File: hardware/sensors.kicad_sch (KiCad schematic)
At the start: 12 parts, among them U5 MMC5983MA, U6 MS560702BA03-50, U7 ADXL375BCCZ, U8 IIM-42653

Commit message: Added digikey part numbers; usb trace width update
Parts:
- C28, C32, C33, C35: Digikey Part Number (none) -> 1276-1857-1-ND
- C29: Digikey Part Number (none) -> 311-1868-1-ND
- C30: Digikey Part Number (none) -> 490-10748-1-ND
- C31: Digikey Part Number (none) -> 478-KGM15AR51E103KTCT-ND
- C34: Digikey Part Number (none) -> 1276-2955-1-ND
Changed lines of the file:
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@@
+			)
+		)
+		(property "Digikey Part Number" "311-1868-1-ND"
+			(at 163.83 63.5 0)
+			(effects
+				(font
+					(size 1.27 1.27)
+				)
+				(hide yes)
 			)
 		)
@@
 			)
 		)
+		(property "Digikey Part Number" "1276-1857-1-ND"
+			(at 153.67 135.89 0)
+			(effects
+				(font
+					(size 1.27 1.27)
+				)
+				(hide yes)
+			)
+		)
 		(pin "1"
 		)
@@
 			)
 		)
+		(property "Digikey Part Number" "1276-2955-1-ND"
+			(at 116.84 132.08 0)
+			(effects
+				(font
+					(size 1.27 1.27)
+				)
+				(hide yes)
+			)
+		)
 		(pin "1"
 		)
@@
 			)
 		)
+		(property "Digikey Part Number" "478-KGM15AR51E103KTCT-ND"
+			(at 97.79 113.03 0)
+			(effects
+				(font
+					(size 1.27 1.27)
+				)
+				(hide yes)
+			)
+		)
 		(pin "1"
 		)
@@
 			)
 		)
+		(property "Digikey Part Number" "1276-1857-1-ND"
+			(at 45.72 60.96 0)
+			(effects
+				(font
+					(size 1.27 1.27)
+				)
+				(hide yes)
+			)
+		)
 		(pin "1"
 		)
@@
 			)
 		)
+		(property "Digikey Part Number" "1276-1857-1-ND"
+			(at 106.68 132.08 0)
+			(effects
+				(font
+					(size 1.27 1.27)
+				)
+				(hide yes)
+			)
+		)
 		(pin "1"
 		)
@@
 			)
 		)
+		(property "Digikey Part Number" "490-10748-1-ND"
+			(at 228.6 68.58 0)
+			(effects
+				(font
+					(size 1.27 1.27)
+				)
+				(hide yes)
+			)
+		)
 		(pin "1"
 		)
@@
 			)
 		)
+		(property "Digikey Part Number" "1276-1857-1-ND"
+			(at 144.78 130.81 0)
+			(effects
+				(font
+					(size 1.27 1.27)
+				)
+				(hide yes)
+			)
+		)

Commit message: Removed bad GND connection to reserved pin on ADXL375 IMU; first error found in first batch
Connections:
- net GND: no longer U7.11 (RESERVED), U7.3 (RESERVED)
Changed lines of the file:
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@@
-	)
-	(junction
-		(at 233.68 137.16)
-		(diameter 0)
-		(color 0 0 0 0)
 	)
 	(junction
@@
 		(color 0 0 0 0)
 	)
-	(junction
-		(at 233.68 139.7)
-		(diameter 0)
-		(color 0 0 0 0)
-	)
 	(wire
 		(pts
@@
 	(wire
 		(pts
-			(xy 233.68 134.62) (xy 233.68 137.16)
+			(xy 233.68 134.62) (xy 233.68 139.7)
 		)
 		(stroke
@@
 	(wire
 		(pts
-			(xy 233.68 137.16) (xy 233.68 139.7)
-		)
-		(stroke
-			(width 0)
-			(type default)
-		)
-	)
-	(wire
-		(pts
 			(xy 29.21 156.21) (xy 30.48 156.21)
 		)
@@
 	(wire
 		(pts
-			(xy 227.33 139.7) (xy 233.68 139.7)
-		)
-		(stroke
-			(width 0)
-			(type default)
-		)
-	)
-	(wire
-		(pts
 			(xy 45.72 55.88) (xy 58.42 55.88)
 		)
@@
 		)
 		(stroke
-			(width 0)
-			(type default)
-		)
-	)
-	(wire
-		(pts
-			(xy 227.33 137.16) (xy 233.68 137.16)
-		)
-		(stroke

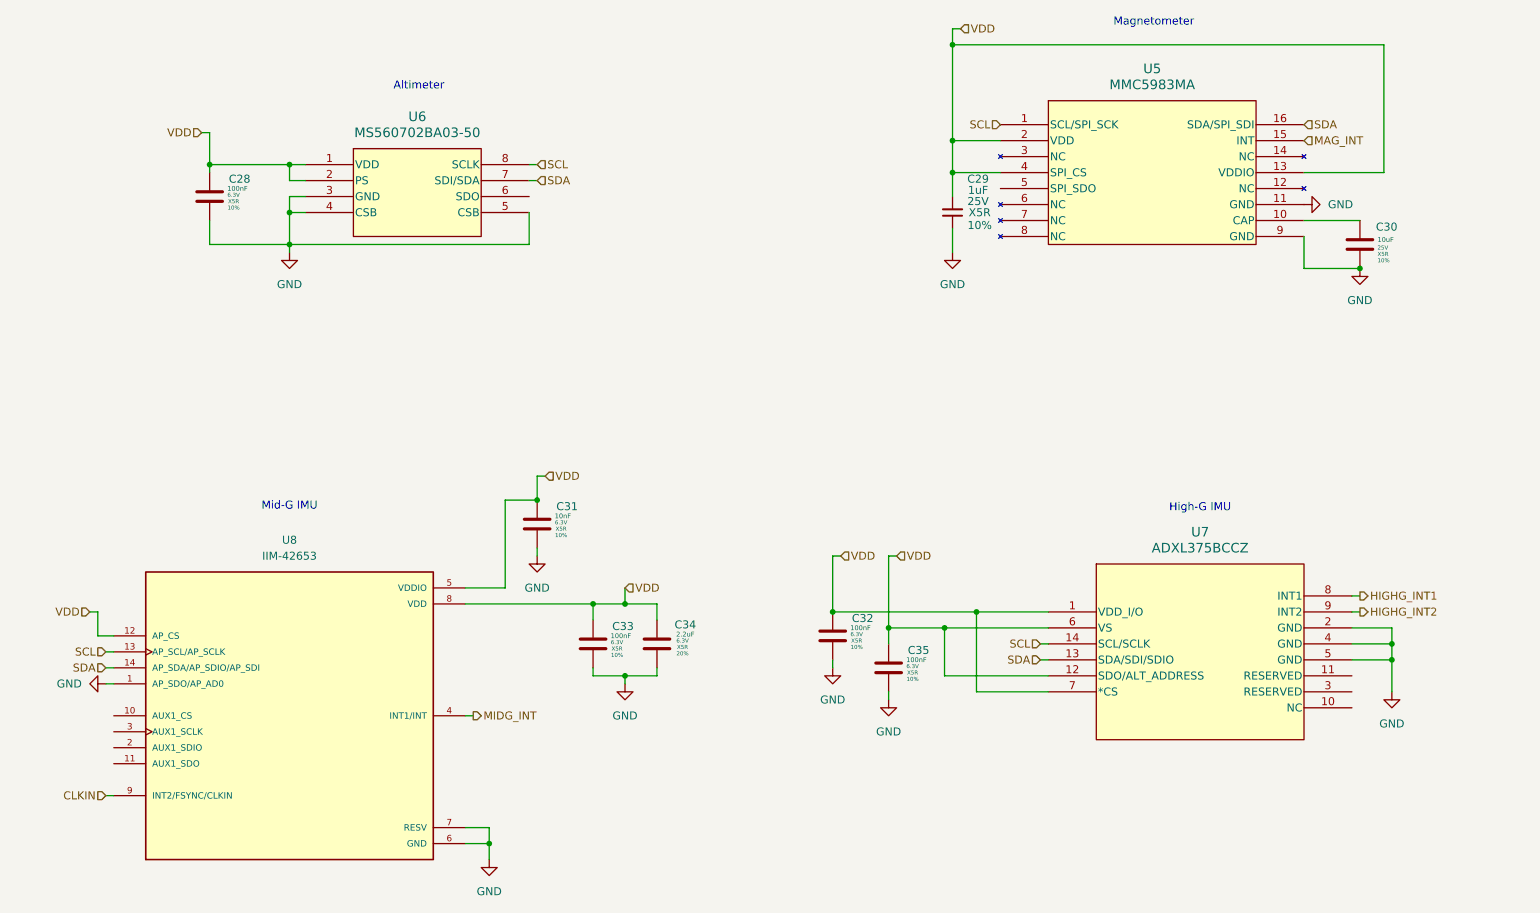
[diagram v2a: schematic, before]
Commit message: Rev 2 of Custom PCB but without Motor Driver (Replaced with Optocoupler Circuit for Standard Servo) (#15)
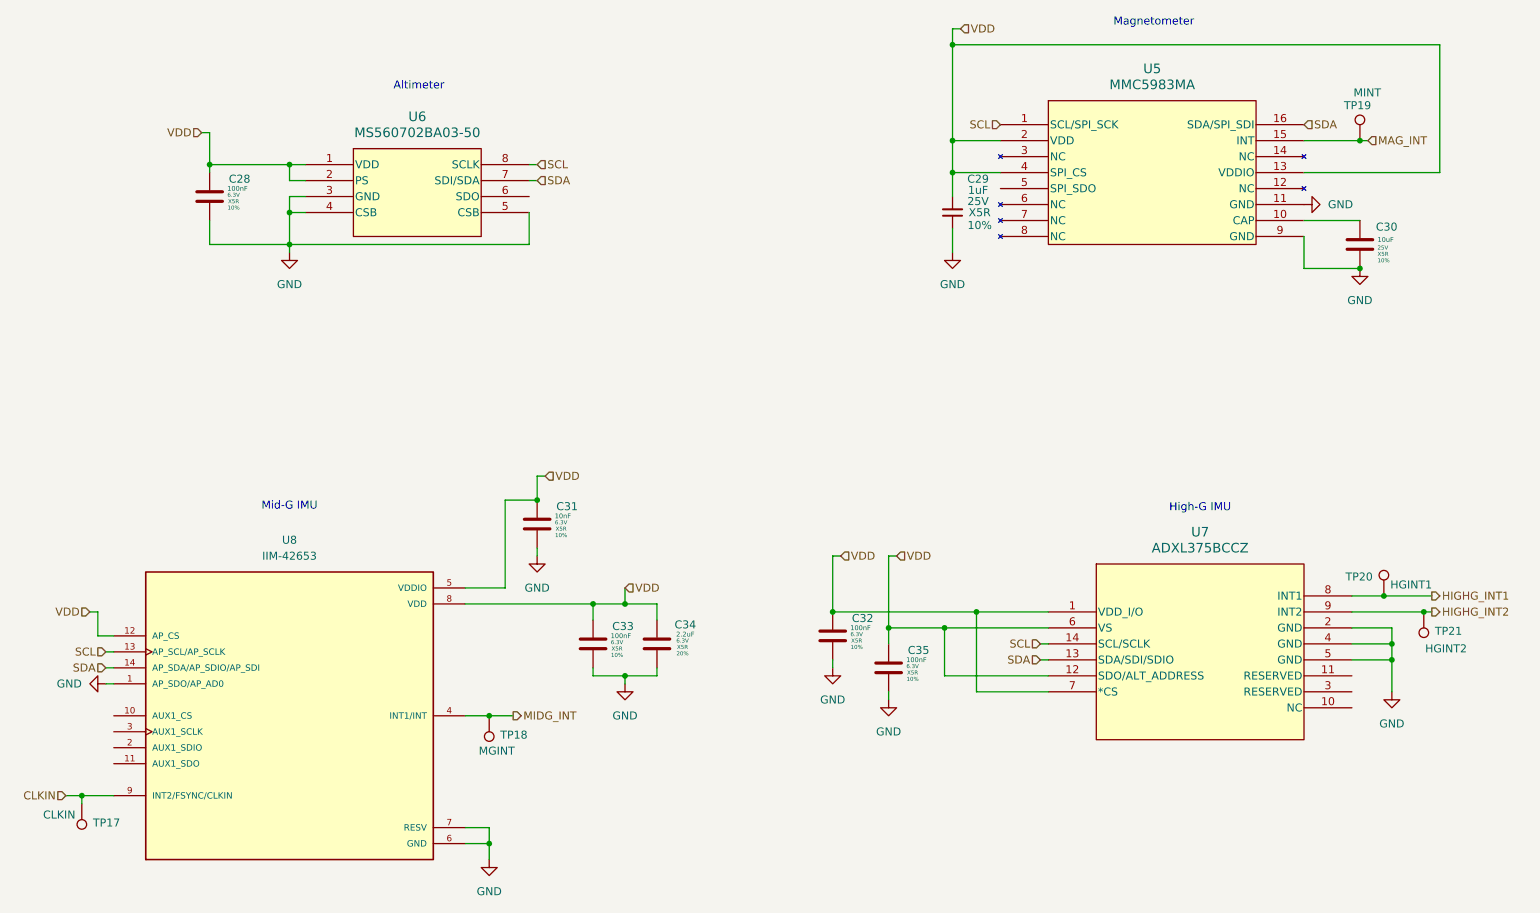
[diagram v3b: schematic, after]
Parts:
- added TP17: CLKIN, TestPoint:TestPoint_Pad_1.0x1.0mm, symbol Connector:TestPoint
- added TP18: MGINT, TestPoint:TestPoint_Pad_1.0x1.0mm, symbol Connector:TestPoint
- added TP19: MINT, TestPoint:TestPoint_Pad_1.0x1.0mm, symbol Connector:TestPoint
- added TP20: HGINT1, TestPoint:TestPoint_Pad_1.0x1.0mm, symbol Connector:TestPoint
- added TP21: HGINT2, TestPoint:TestPoint_Pad_1.0x1.0mm, symbol Connector:TestPoint
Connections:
- net CLKIN: now also TP17.1
- net HIGHG_INT1: now also TP20.1
- net HIGHG_INT2: now also TP21.1
- net MAG_INT: now also TP19.1
- net MIDG_INT: now also TP18.1
